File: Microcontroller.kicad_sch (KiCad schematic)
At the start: 26 parts, among them J1 GT-USB-7010ASV, SW2 KMR231NG, SW3 KMR231NG, U1 ESP32-S3-MINI-1

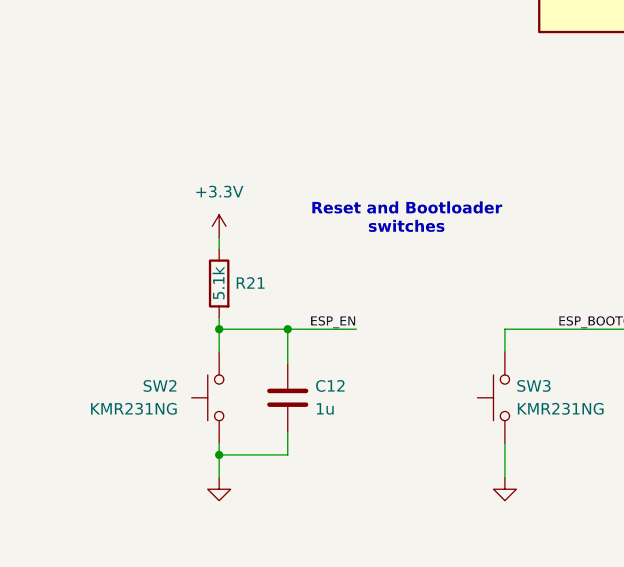
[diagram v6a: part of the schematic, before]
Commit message: For design review X01-001 Ammendment: Changed ALL VIAS to 0.3/0.55 to reduce fab cost. Signed-off-by: James Mendel <jrm.mendel@gmail.com>
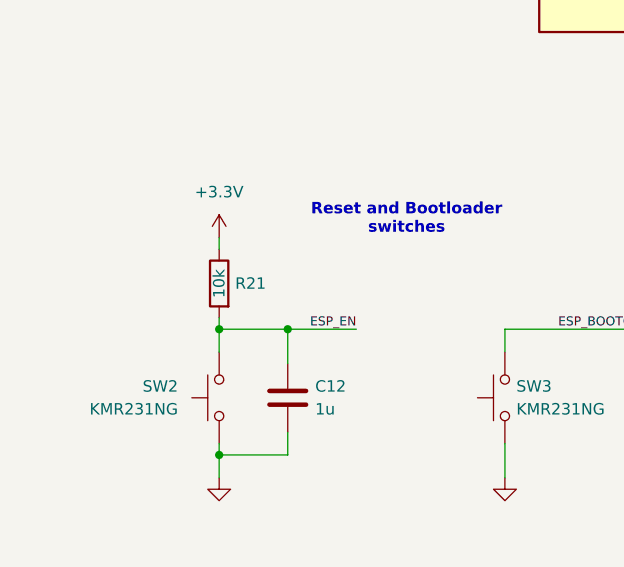
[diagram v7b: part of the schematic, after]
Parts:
- C1: MPN (none) -> CL10A226MP8NUNE
- C12: MPN (none) -> CL10A105KO8NNNC
- C2: MPN (none) -> CL10B104KO8NNNC
- R15, R16, R2, R3: MPN (none) -> RC0603FR-075K1L
- R21: value 5.1k -> 10k; MPN (none) -> RC0603FR-0710KL
- R26: MPN (none) -> RC0603FR-071K5L
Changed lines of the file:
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@@
 			)
 		)
-		(property "Value" "5.1k"
+		(property "Value" "10k"
 			(at 35.56 152.4 90)
 			(effects
@@
 			)
 		)
-		(property "Datasheet" "~"
+		(property "Datasheet" "https://www.lcsc.com/datasheet/lcsc_datasheet_2304140030_YAGEO-RC0603FR-071KL_C22548.pdf"
 			(at 35.56 152.4 0)
 			(effects
@@
 		)
 		(property "Description" "Resistor"
+			(at 35.56 152.4 0)
+			(effects
+				(font
+					(size 1.27 1.27)
+				)
+				(hide yes)
+			)
+		)
+		(property "MPN" "RC0603FR-0710KL"
 			(at 35.56 152.4 0)
 			(effects
@@
 			)
 		)
-		(property "Datasheet" "~"
+		(property "Datasheet" "https://www.lcsc.com/datasheet/lcsc_datasheet_2304140030_YAGEO-RC0603FR-071KL_C22548.pdf"
 			(at 201.93 109.22 0)
 			(effects
@@
 		)
 		(property "Description" "Resistor"
+			(at 201.93 109.22 0)
+			(effects
+				(font
+					(size 1.27 1.27)
+				)
+				(hide yes)
+			)
+		)
+		(property "MPN" "RC0603FR-071K5L"
 			(at 201.93 109.22 0)
 			(effects
@@
 			)
 		)
+		(property "MPN" "CL10A226MP8NUNE"
+			(at 147.32 39.37 0)
+			(effects
+				(font
+					(size 1.27 1.27)
+				)
+				(hide yes)
+			)
+		)
 		(pin "1"
 		)
@@
 			)
 		)
-		(property "Datasheet" "~"
+		(property "Datasheet" "https://www.lcsc.com/datasheet/lcsc_datasheet_2304140030_YAGEO-RC0603FR-071KL_C22548.pdf"
 			(at 38.1 78.74 0)
 			(effects
@@
 		)
 		(property "Description" "Resistor"
+			(at 38.1 78.74 0)
+			(effects
+				(font
+					(size 1.27 1.27)
+				)
+				(hide yes)
+			)
+		)
+		(property "MPN" "RC0603FR-075K1L"
 			(at 38.1 78.74 0)
 			(effects
@@
 			)
 		)
-		(property "Datasheet" "~"
+		(property "Datasheet" "https://www.lcsc.com/datasheet/lcsc_datasheet_2304140030_YAGEO-RC0603FR-071KL_C22548.pdf"
 			(at 228.6 57.15 0)
 			(effects
@@
 		)
 		(property "Description" "Resistor"
+			(at 228.6 57.15 0)
+			(effects
+				(font
+					(size 1.27 1.27)
+				)
+				(hide yes)
+			)
+		)
+		(property "MPN" "RC0603FR-075K1L"
 			(at 228.6 57.15 0)
 			(effects
@@
 			)
 		)
+		(property "MPN" "CL10B104KO8NNNC"
+			(at 137.16 39.37 0)
+			(effects
+				(font
+					(size 1.27 1.27)
+				)
+				(hide yes)
+			)
+		)
 		(pin "1"
 		)
@@
 			)
 		)
-		(property "Datasheet" "~"
+		(property "Datasheet" "https://www.lcsc.com/datasheet/lcsc_datasheet_2304140030_YAGEO-RC0603FR-071KL_C22548.pdf"
 			(at 43.18 78.74 0)
 			(effects
@@
 		)
 		(property "Description" "Resistor"
+			(at 43.18 78.74 0)
+			(effects
+				(font
+					(size 1.27 1.27)
+				)
+				(hide yes)
+			)
+		)
+		(property "MPN" "RC0603FR-075K1L"
 			(at 43.18 78.74 0)
 			(effects
@@
 			)
 		)
-		(property "Datasheet" "~"
+		(property "Datasheet" "https://www.lcsc.com/datasheet/lcsc_datasheet_2304140030_YAGEO-RC0603FR-071KL_C22548.pdf"
 			(at 228.6 54.61 0)
 			(effects
@@
 		)
 		(property "Description" "Resistor"
+			(at 228.6 54.61 0)
+			(effects
+				(font
+					(size 1.27 1.27)
+				)
+				(hide yes)
+			)
+		)
+		(property "MPN" "RC0603FR-075K1L"
 			(at 228.6 54.61 0)
 			(effects
@@
 			(at 43.18 165.1 0)
 			(effects
+				(font
+					(size 1.27 1.27)
+				)
+				(hide yes)
+			)
+		)
+		(property "MPN" "CL10A105KO8NNNC"
+			(at 43.18 165.1 0)
+			(effects

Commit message: Release X01-003 - Added "JRM" logo to L3 and and Modem Works logo to L4. - Upated copyright - Added alternates for some components - Some cleanup on SCH and PCB.
Signed-off-by: James Mendel <jrm.mendel@gmail.com>
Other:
- company: J. MENDEL -> ${COMPANY}
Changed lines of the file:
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@@
 	(title_block
 		(title "${TITLE}")
-		(date "2025-04-05")
+		(date "2025-04-06")
 		(rev "${REVISION}")
-		(company "J. MENDEL")
+		(company "${COMPANY}")
+		(comment 1 "${LICENSE}")
+		(comment 2 "${COPYRIGHT}")
 	)
 	(rectangle
@@
 	(text_box "Sheet: ${SHEETNAME}"
 		(exclude_from_sim no)
-		(at 177.8 167.64 0)
-		(size 106.68 12.7)
+		(at 213.36 167.64 0)
+		(size 71.12 12.7)
 		(margins 0.9525 0.9525 0.9525 0.9525)
 		(stroke
